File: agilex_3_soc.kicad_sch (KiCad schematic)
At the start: 11 parts, among them J1 Conn_01x14, J2 Conn_02x03_Odd_Even, J3 Conn_02x19_Odd_Even, J4 Conn_01x03, J5 Conn_01x03, J6 Micro_SD_Card, J7 8P8C_LED_Shielded, U1 IS43LQ32256A-062BLI, U2 ADS7886xxDBV, U3 CD4051B, Y1 ASDMB-25MHz

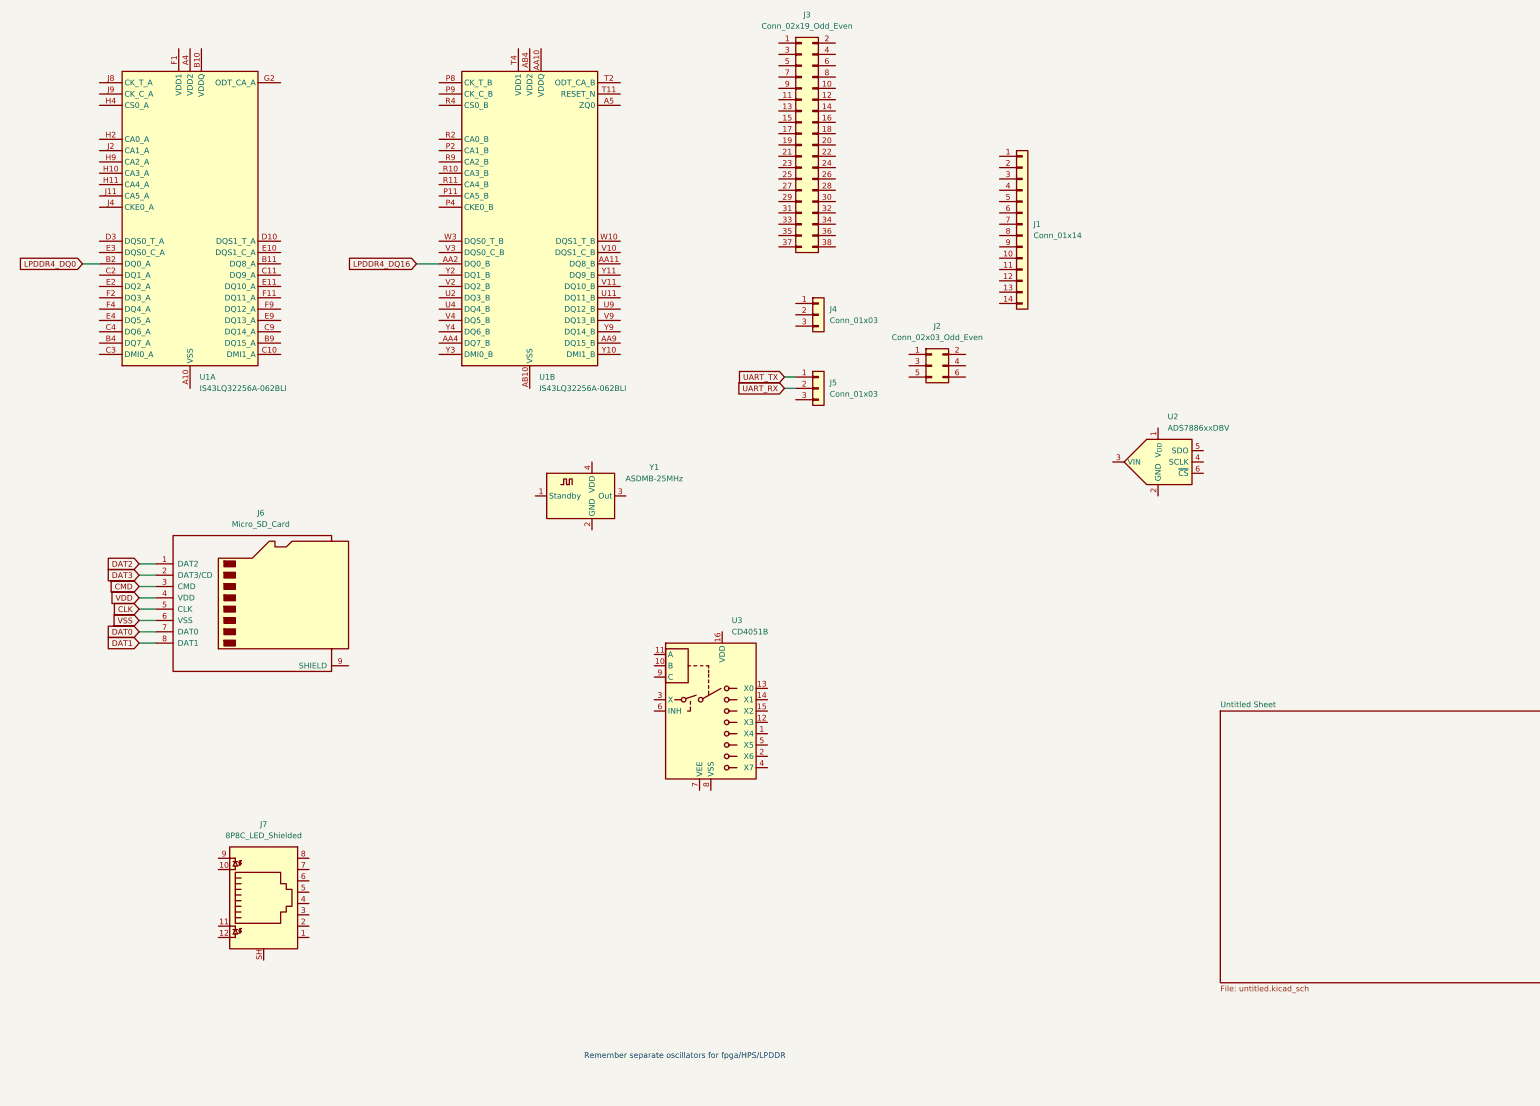
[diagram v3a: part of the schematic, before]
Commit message: add lpddr4 connections in schematic
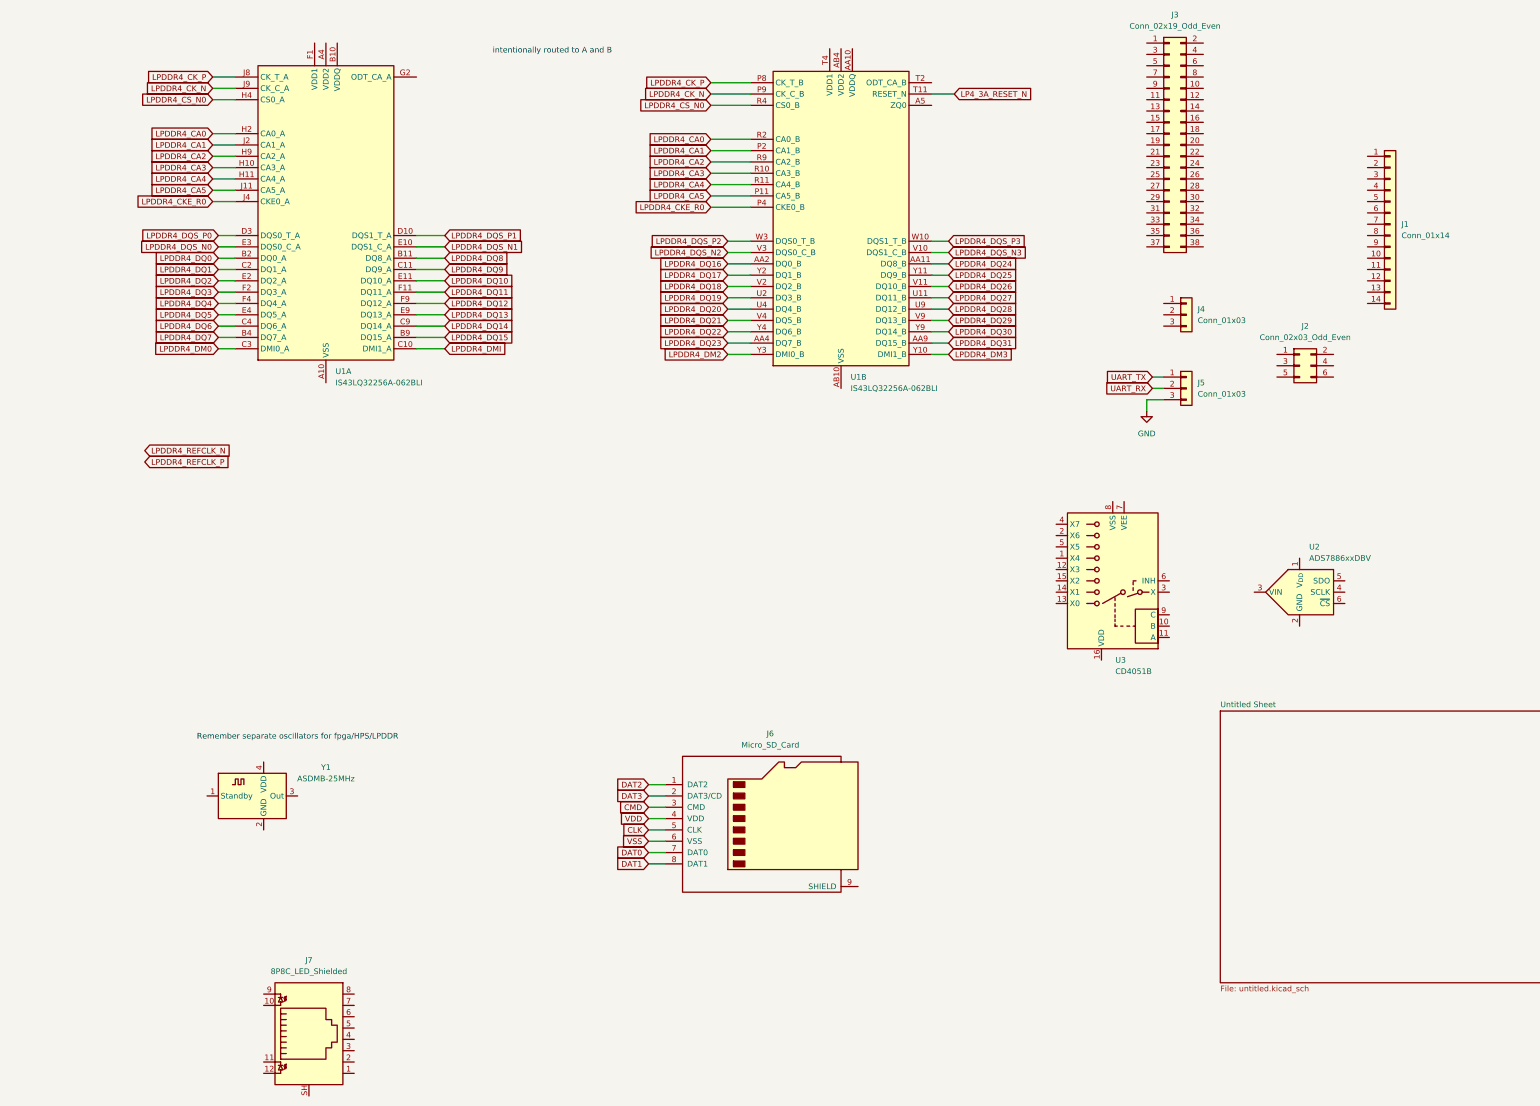
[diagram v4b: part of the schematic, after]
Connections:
- net LPDDR4_DQ24: now reaches U1.AA11 (DQ8_B)
- net LPDDR4_DQ23: now reaches U1.AA4 (DQ7_B)
- net LPDDR4_DQ31: now reaches U1.AA9 (DQ15_B)
- net LPDDR4_CA5: now reaches U1.P11 (CA5_B)
- net LPDDR4_CA5: now also U1.J11 (CA5_A)
- net LPDDR4_CA1: now reaches U1.P2 (CA1_B)
- net LPDDR4_CA1: now also U1.J2 (CA1_A)
- net LPDDR4_CKE_R0: now reaches U1.P4 (CKE0_B)
- net LPDDR4_CKE_R0: now also U1.J4 (CKE0_A)
- net LPDDR4_CK_P: now reaches U1.P8 (CK_T_B)
- net LPDDR4_CK_P: now also U1.J8 (CK_T_A)
- net LPDDR4_CK_N: now reaches U1.P9 (CK_C_B)
- net LPDDR4_CK_N: now also U1.J9 (CK_C_A)
- net LPDDR4_CA3: now reaches U1.R10 (CA3_B)
- net LPDDR4_CA3: now also U1.H10 (CA3_A)
- net LPDDR4_CA4: now reaches U1.R11 (CA4_B)
- net LPDDR4_CA4: now also U1.H11 (CA4_A)
- net LPDDR4_CA0: now reaches U1.R2 (CA0_B)
- net LPDDR4_CA0: now also U1.H2 (CA0_A)
- net LPDDR4_CS_N0: now reaches U1.R4 (CS0_B)
- net LPDDR4_CS_N0: now also U1.H4 (CS0_A)
- net LPDDR4_CA2: now reaches U1.R9 (CA2_B)
- net LPDDR4_CA2: now also U1.H9 (CA2_A)
- net LP4_3A_RESET_N: now reaches U1.T11 (RESET_N)
- net LPDDR4_DQ27: now reaches U1.U11 (DQ11_B)
- net LPDDR4_DQ19: now reaches U1.U2 (DQ3_B)
- net LPDDR4_DQ20: now reaches U1.U4 (DQ4_B)
- net LPDDR4_DQ28: now reaches U1.U9 (DQ12_B)
- net LPDDR4_DQS_N3: now reaches U1.V10 (DQS1_C_B)
- net LPDDR4_DQ26: now reaches U1.V11 (DQ10_B)
- net LPDDR4_DQ18: now reaches U1.V2 (DQ2_B)
- net LPDDR4_DQS_N2: now reaches U1.V3 (DQS0_C_B)
- net LPDDR4_DQ21: now reaches U1.V4 (DQ5_B)
- net LPDDR4_DQ29: now reaches U1.V9 (DQ13_B)
- net LPDDR4_DQS_P3: now reaches U1.W10 (DQS1_T_B)
- net LPDDR4_DQS_P2: now reaches U1.W3 (DQS0_T_B)
- net LPDDR4_DM3: now reaches U1.Y10 (DMI1_B)
- net LPDDR4_DQ25: now reaches U1.Y11 (DQ9_B)
- net LPDDR4_DQ17: now reaches U1.Y2 (DQ1_B)
- net LPDDR4_DM2: now reaches U1.Y3 (DMI0_B)
- net LPDDR4_DQ22: now reaches U1.Y4 (DQ6_B)
- net LPDDR4_DQ30: now reaches U1.Y9 (DQ14_B)
- net LPDDR4_DQ8: now reaches U1.B11 (DQ8_A)
- net LPDDR4_DQ7: now reaches U1.B4 (DQ7_A)
- net LPDDR4_DQ15: now reaches U1.B9 (DQ15_A)
- net LPDDR4_DMI: now reaches U1.C10 (DMI1_A)
- net LPDDR4_DQ9: now reaches U1.C11 (DQ9_A)
- net LPDDR4_DQ1: now reaches U1.C2 (DQ1_A)
- net LPDDR4_DM0: now reaches U1.C3 (DMI0_A)
- net LPDDR4_DQ6: now reaches U1.C4 (DQ6_A)
- net LPDDR4_DQ14: now reaches U1.C9 (DQ14_A)
- net LPDDR4_DQS_P1: now reaches U1.D10 (DQS1_T_A)
- net LPDDR4_DQS_P0: now reaches U1.D3 (DQS0_T_A)
- net LPDDR4_DQS_N1: now reaches U1.E10 (DQS1_C_A)
- net LPDDR4_DQ10: now reaches U1.E11 (DQ10_A)
- net LPDDR4_DQ2: now reaches U1.E2 (DQ2_A)
- net LPDDR4_DQS_N0: now reaches U1.E3 (DQS0_C_A)
- net LPDDR4_DQ5: now reaches U1.E4 (DQ5_A)
- net LPDDR4_DQ13: now reaches U1.E9 (DQ13_A)
- net LPDDR4_DQ11: now reaches U1.F11 (DQ11_A)
- net LPDDR4_DQ3: now reaches U1.F2 (DQ3_A)
- net LPDDR4_DQ4: now reaches U1.F4 (DQ4_A)
- net LPDDR4_DQ12: now reaches U1.F9 (DQ12_A)
- net GND: now reaches J5.3 (Pin_3)
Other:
- note added: "intentionally routed to A and B"
- moved on the sheet: J1, J2, J3, J4, J5, J6, J7, U1A, U1B, U2, U3, Y1

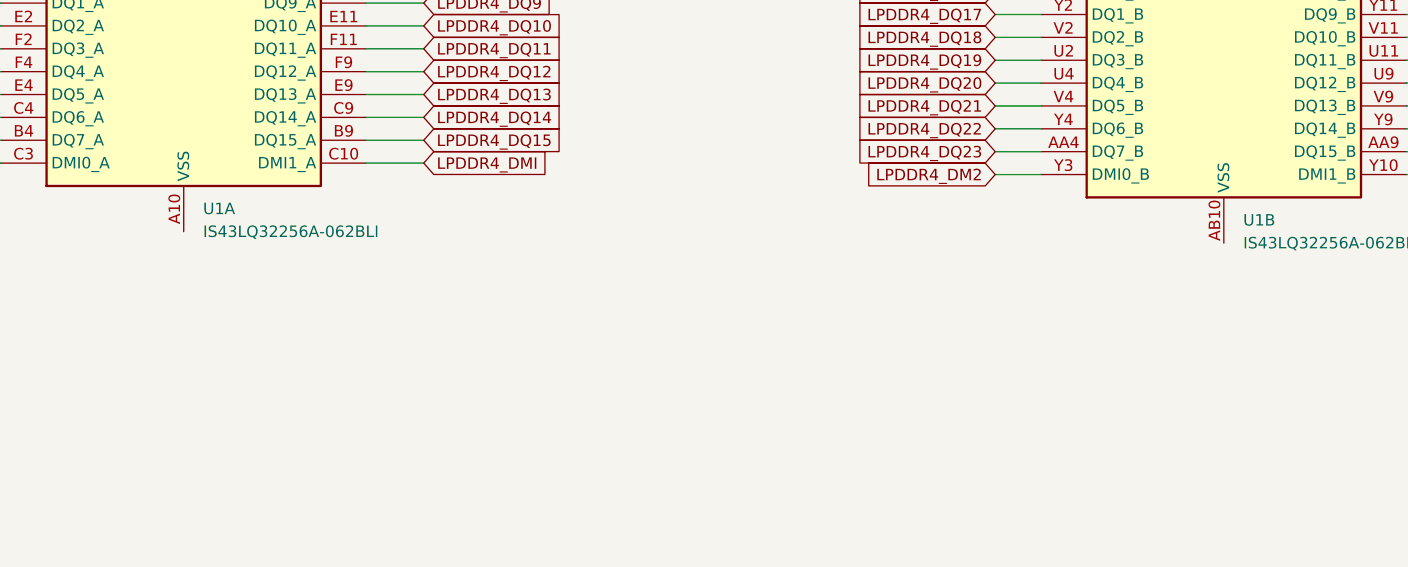
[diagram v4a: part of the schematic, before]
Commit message: start making agilex 5 b23b package
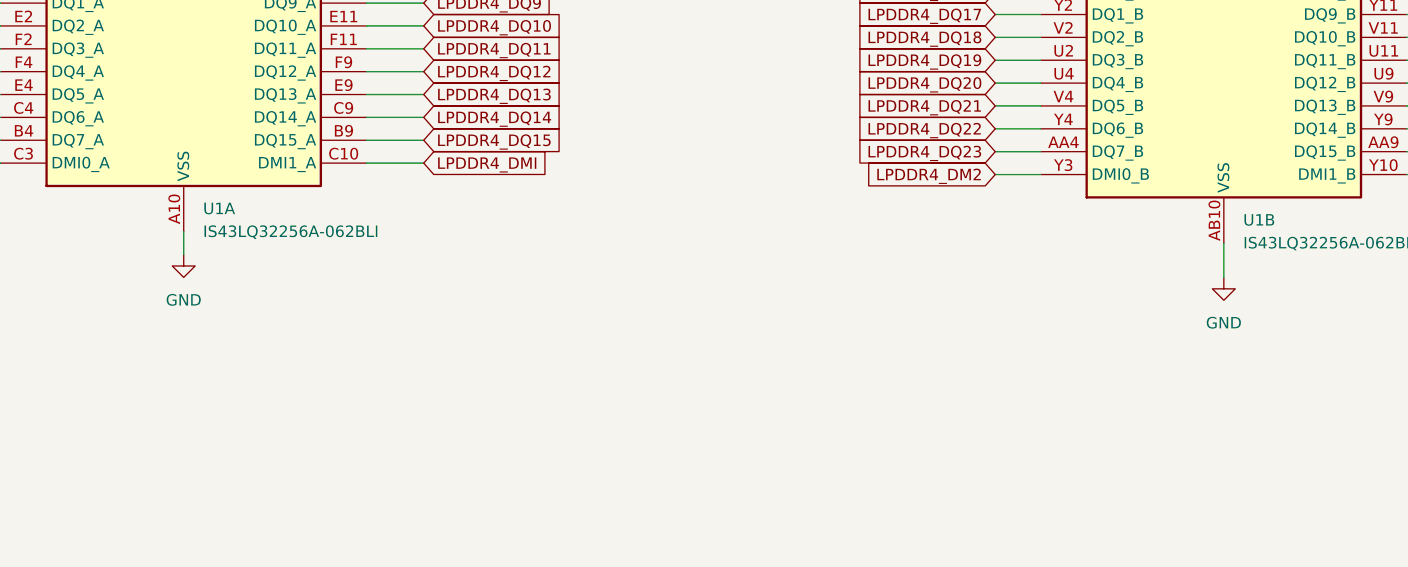
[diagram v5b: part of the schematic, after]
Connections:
- net GND: now also U1.A10 (VSS), U1.A3 (VSS), U1.AB10 (VSS), U1.AB3 (VSS), U1.AB5 (VSS), U1.AB8 (VSS), U1.C1 (VSS), U1.C12 (VSS), U1.C5 (VSS), U1.C8 (VSS), U1.D11 (VSS), U1.D2 (VSS), U1.D4 (VSS), U1.D9 (VSS), U1.E1 (VSS), U1.E12 (VSS), U1.E5 (VSS), U1.E8 (VSS), U1.G1 (VSS), U1.G10 (VSS), U1.G12 (VSS), U1.G3 (VSS), U1.G5 (VSS), U1.G8 (VSS), U1.J1 (VSS), U1.J10 (VSS), U1.J12 (VSS), U1.J3 (VSS), U1.K11 (VSS), U1.K2 (VSS), U1.K4 (VSS), U1.K9 (VSS), U1.N11 (VSS), U1.N2 (VSS), U1.N4 (VSS), U1.N9 (VSS), U1.P1 (VSS), U1.P10 (VSS), U1.P12 (VSS), U1.P3 (VSS), U1.T1 (VSS), U1.T10 (VSS), U1.T12 (VSS), U1.T3 (VSS), U1.T5 (VSS), U1.T8 (VSS), U1.V1 (VSS), U1.V12 (VSS), U1.V5 (VSS), U1.V8 (VSS), U1.W11 (VSS), U1.W2 (VSS), U1.W4 (VSS), U1.W9 (VSS), U1.Y1 (VSS), U1.Y12 (VSS), U1.Y5 (VSS), U1.Y8 (VSS)
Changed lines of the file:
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@@
 	(wire
 		(pts
+			(xy 213.36 107.95) (xy 213.36 111.76)
+		)
+		(stroke
+			(width 0)
+			(type default)
+		)
+	)
+	(wire
+		(pts
 			(xy 118.11 99.06) (xy 124.46 99.06)
 		)
@@
 	(wire
 		(pts
+			(xy 97.79 106.68) (xy 97.79 109.22)
+		)
+		(stroke
+			(width 0)
+			(type default)
+		)
+	)
+	(wire
+		(pts
 			(xy 187.96 82.55) (xy 193.04 82.55)
 		)
@@
 	)
 	(symbol
+		(lib_id "power:GND")
+		(at 213.36 111.76 0)
+		(unit 1)
+		(exclude_from_sim no)
+		(in_bom yes)
+		(on_board yes)
+		(dnp no)
+		(fields_autoplaced yes)
+		(property "Reference" "#PWR05"
+			(at 213.36 118.11 0)
+			(effects
+				(font
+					(size 1.27 1.27)
+				)
+				(hide yes)
+			)
+		)
+		(property "Value" "GND"
+			(at 213.36 116.84 0)
+			(effects
+				(font
+					(size 1.27 1.27)
+				)
+			)
+		)
+		(property "Footprint" ""
+			(at 213.36 111.76 0)
+			(effects
+				(font
+					(size 1.27 1.27)
+				)
+				(hide yes)
+			)
+		)
+		(property "Datasheet" ""
+			(at 213.36 111.76 0)
+			(effects
+				(font
+					(size 1.27 1.27)
+				)
+				(hide yes)
+			)
+		)
+		(property "Description" "Power symbol creates a global label with name \"GND\" , ground"
+			(at 213.36 111.76 0)
+			(effects
+				(font
+					(size 1.27 1.27)
+				)
+				(hide yes)
+			)
+		)
+		(pin "1"
+		)
+		(instances
+			(project ""
+				(path "/a5b98d95-6877-4284-904f-d04e32723ae0"
+					(reference "#PWR05")
+					(unit 1)
+				)
+			)
+		)
+	)
+	(symbol
 		(lib_id "Analog_ADC:ADS7886xxDBV")
 		(at 316.23 153.67 0)
@@
 					(unit 1)
 				)
+			)
+		)
+	)
+	(symbol
+		(lib_id "power:GND")
+		(at 97.79 109.22 0)
+		(unit 1)
+		(exclude_from_sim no)
+		(in_bom yes)
+		(on_board yes)
+		(dnp no)
+		(fields_autoplaced yes)
+		(property "Reference" "#PWR04"
+			(at 97.79 115.57 0)
+			(effects
+				(font
+					(size 1.27 1.27)
+				)
+				(hide yes)
+			)
+		)
+		(property "Value" "GND"
+			(at 97.79 114.3 0)
+			(effects
+				(font
+					(size 1.27 1.27)
+				)
+			)
+		)
+		(property "Footprint" ""
+			(at 97.79 109.22 0)
+			(effects
+				(font
+					(size 1.27 1.27)
+				)
+				(hide yes)
+			)
+		)
+		(property "Datasheet" ""
+			(at 97.79 109.22 0)
+			(effects
+				(font
+					(size 1.27 1.27)
+				)
+				(hide yes)
+			)
+		)
+		(property "Description" "Power symbol creates a global label with name \"GND\" , ground"
+			(at 97.79 109.22 0)
+			(effects
+				(font
+					(size 1.27 1.27)
+				)
+				(hide yes)
+			)
+		)
+		(pin "1"
+		)
+		(instances
+			(project ""
+				(path "/a5b98d95-6877-4284-904f-d04e32723ae0"
+					(reference "#PWR04")
+					(unit 1)
+				)

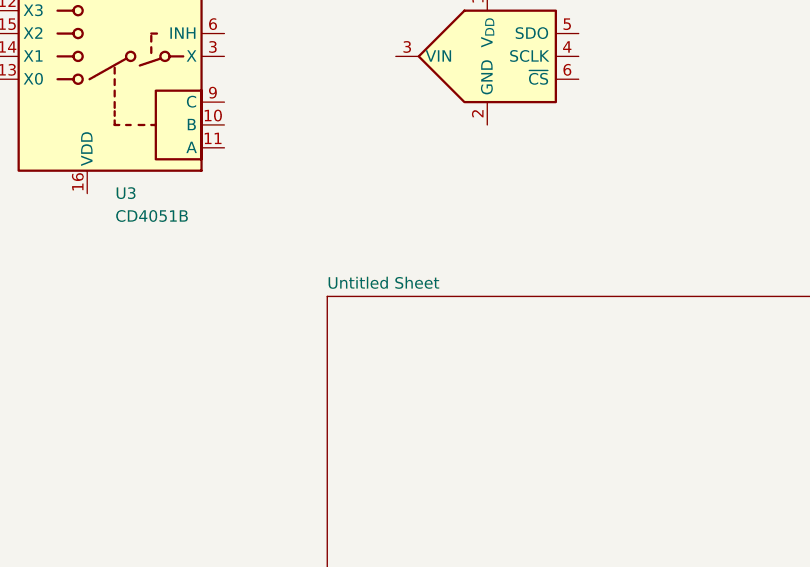
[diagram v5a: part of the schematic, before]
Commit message: even more balls in b23b package
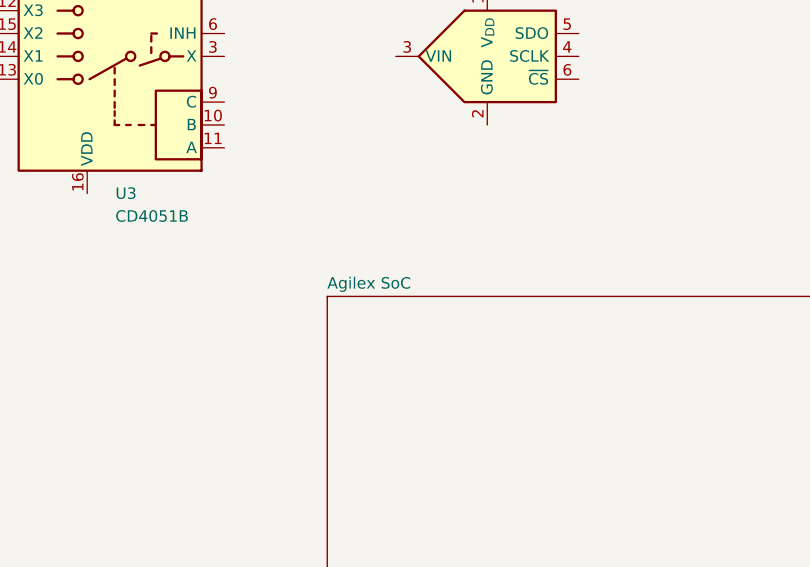
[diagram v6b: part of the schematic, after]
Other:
- sheet Untitled Sheet renamed Agilex SoC
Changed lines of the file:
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@@
 			(color 0 0 0 0.0000)
 		)
-		(property "Sheetname" "Untitled Sheet"
+		(property "Sheetname" "Agilex SoC"
 			(at 298.45 179.6284 0)
 			(effects

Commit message: start creating schematic symbol for agilex 5
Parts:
- added R3, R4, R5, R6, R7, R8, R9: 240R, Capacitor_SMD:C_0402_1005Metric, symbol Device:R
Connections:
- net GND: now also R3.1, R4.1, R5.1, R6.1, R7.1, R8.1, R9.1
- new net t1: R9.2
- new net t2: R8.2
- new net t3: R7.2
- new net t4: R6.2
- new net t5: R5.2
- new net t6: R4.2
- new net t7: R3.2
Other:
- sheet Agilex SoC ports: added p1; removed none
- moved on the sheet: J6

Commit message: add agilex 5 schematic files
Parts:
- renumbered U1 to U5
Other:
- added sheet Connectors (a5e_kicad/connectors.kicad_sch)
- added sheet Ethernet Phy (a5e_kicad/eth.kicad_sch)
- added sheet FPGA gnd (a5e_kicad/fpga_gnd.kicad_sch)
- added sheet FPGA power (a5e_kicad/fpga_power.kicad_sch)
- added sheet HPS (a5e_kicad/hps.kicad_sch)
- added sheet IOBANK 2 (a5e_kicad/iobank2.kicad_sch)
- added sheet IOBANK 3 (a5e_kicad/iobank3.kicad_sch)
- added sheet IOBANK6ab (a5e_kicad/iobank6ab.kicad_sch)
- added sheet IOBANK6cd (a5e_kicad/iobank6cd.kicad_sch)
- added sheet IOBANK6ef (a5e_kicad/iobank6ef.kicad_sch)
- added sheet IOBANK6gh (a5e_kicad/iobank6gh.kicad_sch)
- added sheet SDM (a5e_kicad/sdm.kicad_sch)
- added sheet clock (a5e_kicad/clk.kicad_sch)
- added sheet hybperbus (a5e_kicad/hyperbus.kicad_sch)
- added sheet lpddr4 memory (a5e_kicad/mem1.kicad_sch)
- added sheet power supply (a5e_kicad/ps.kicad_sch)
- added sheet power supply1 (a5e_kicad/ps1.kicad_sch)
- added sheet usb (a5e_kicad/usb.kicad_sch)
- note added: "1.1V"
- note added: "1.8V"
- note added: "Core Voltage"
- note added: "Peripheral Voltages"
